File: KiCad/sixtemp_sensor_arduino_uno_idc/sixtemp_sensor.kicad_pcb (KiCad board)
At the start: 2 copper layers, 53.3 x 68.6 mm, 44 parts, among them J10 debug, J12 Sig_conn, J123456 Led_EN, J13 RB_Conn, J31 1-Wire, J32 1-Wire, J33 1-Wire, J34 1-Wire, J35 1-Wire, J36 1-Wire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

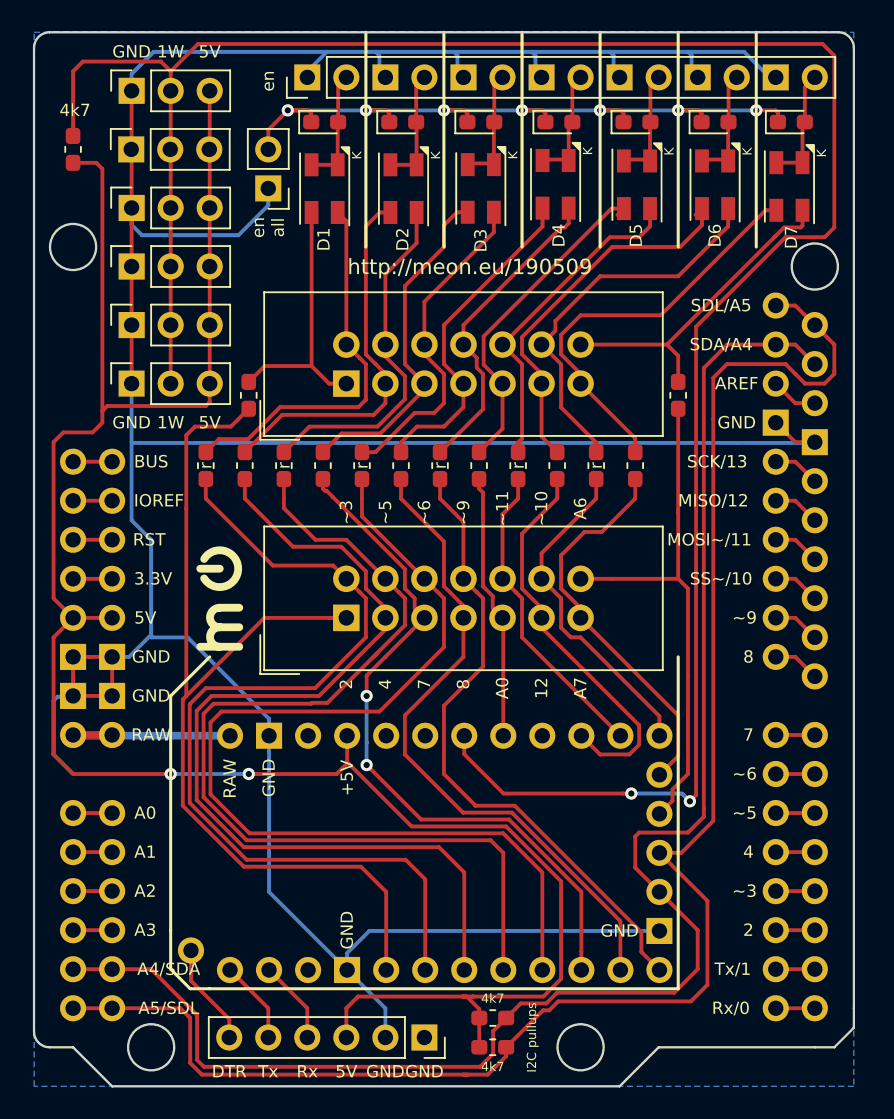
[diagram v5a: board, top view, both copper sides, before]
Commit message: A6→A3, A7→A2 and set as alarm
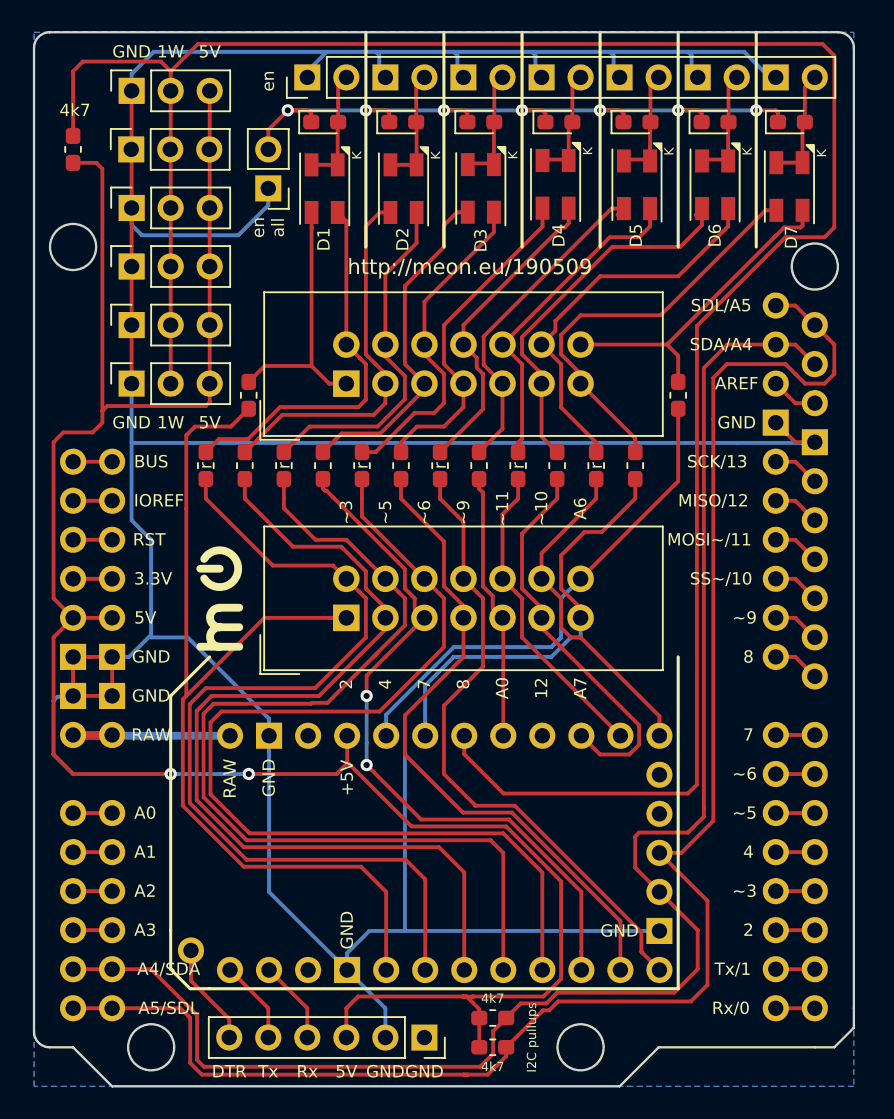
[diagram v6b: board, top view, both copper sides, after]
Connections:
- J12 pad 13: A7 -> A2
- J12 pad 14: A6 -> A3
- R71 pad 2: A6 -> A3
- R72 pad 2: A7 -> A2
- U1 pad 19: A6 -> Net-(U1-Pad19)
- U1 pad 22: A7 -> Net-(U1-Pad22)
- U1 pad 25: Net-(U1-Pad25) -> A2
- U1 pad 26: Net-(U1-Pad26) -> A3
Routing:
- net A6: track 33.9 -> 0.00 mm
- net A3: track 0.00 -> 32.9 mm
- net A2: track 0.00 -> 28.9 mm
- net A7: track 26.3 -> 0.00 mm
- net GND: track 230.2 -> 244.2 mm
- net 1wire: track 147.5 -> 145.9 mm, vias 2 -> 0

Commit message: draw lines between connected pin holes
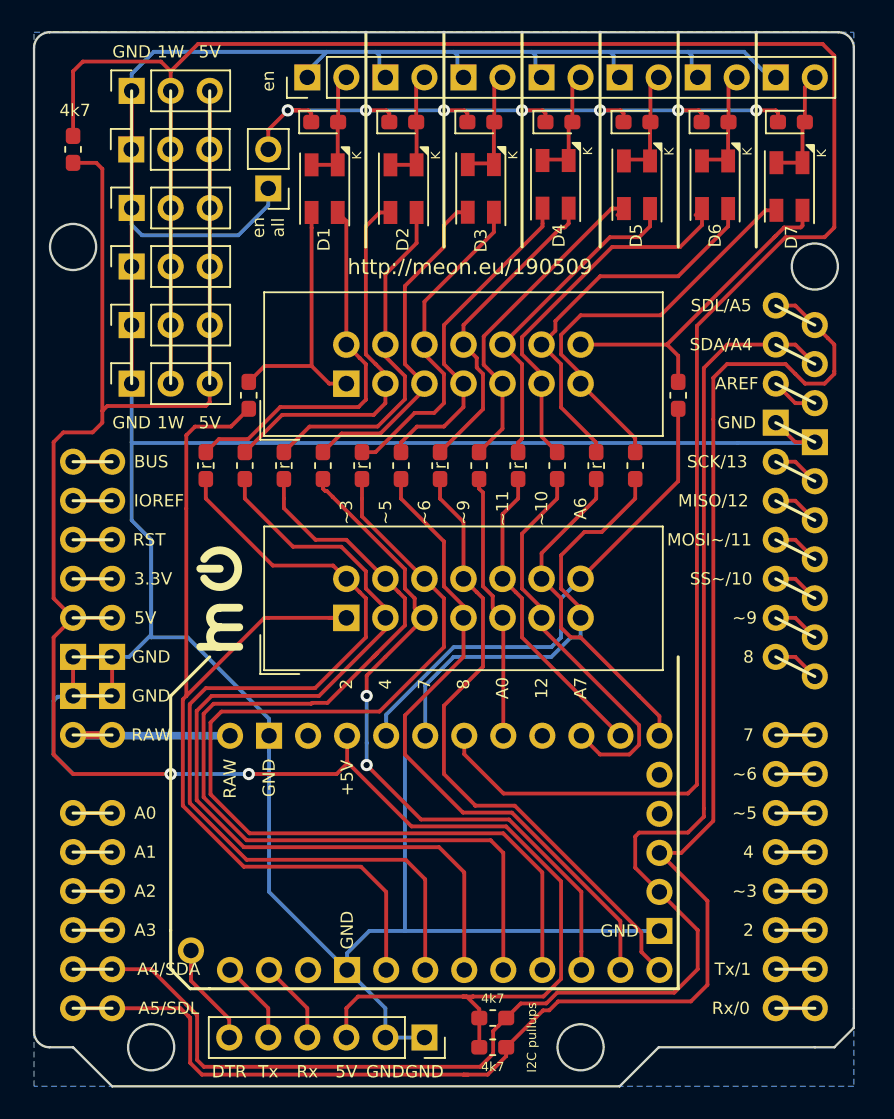
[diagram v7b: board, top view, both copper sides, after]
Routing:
- net GND: track 244.2 -> 246.7 mm
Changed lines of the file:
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@@
   (general
     (thickness 1.6)
-    (drawings 85)
-    (tracks 637)
+    (drawings 120)
+    (tracks 638)
     (zones 0)
     (modules 44)
@@
     (visible_elements FFFFFF7F)
     (pcbplotparams
-      (layerselection 0x010fc_ffffffff)
+      (layerselection 0x010a8_7fffffff)
       (usegerberextensions false)
       (usegerberattributes false)
@@
     )
   )
+  (gr_line (start 68.58 96.52) (end 71.12 96.52) (layer F.SilkS) (width 0.2))
+  (gr_line (start 68.58 93.98) (end 71.12 93.98) (layer F.SilkS) (width 0.2))
+  (gr_line (start 68.58 91.44) (end 71.12 91.44) (layer F.SilkS) (width 0.2))
+  (gr_line (start 68.58 88.9) (end 71.12 88.9) (layer F.SilkS) (width 0.2))
+  (gr_line (start 68.58 86.36) (end 71.12 86.36) (layer F.SilkS) (width 0.2))
+  (gr_line (start 68.58 83.82) (end 71.12 83.82) (layer F.SilkS) (width 0.2))
+  (gr_line (start 114.3 50.8) (end 116.84 52.07) (layer F.SilkS) (width 0.2))
+  (gr_line (start 114.3 53.34) (end 116.84 54.61) (layer F.SilkS) (width 0.2))
+  (gr_line (start 114.3 55.88) (end 116.84 57.15) (layer F.SilkS) (width 0.2))
+  (gr_line (start 114.3 58.42) (end 116.84 59.69) (layer F.SilkS) (width 0.2))
+  (gr_line (start 114.3 60.96) (end 116.84 62.23) (layer F.SilkS) (width 0.2))
+  (gr_line (start 114.3 63.5) (end 116.84 64.77) (layer F.SilkS) (width 0.2))
+  (gr_line (start 114.3 66.04) (end 116.84 67.31) (layer F.SilkS) (width 0.2))
+  (gr_line (start 114.3 68.58) (end 116.84 69.85) (layer F.SilkS) (width 0.2))
+  (gr_line (start 114.3 71.12) (end 116.84 72.39) (layer F.SilkS) (width 0.2))
+  (gr_line (start 114.3 73.66) (end 116.84 74.93) (layer F.SilkS) (width 0.2))
+  (gr_line (start 114.3 78.74) (end 116.84 78.74) (layer F.SilkS) (width 0.2))
+  (gr_line (start 114.3 81.28) (end 116.84 81.28) (layer F.SilkS) (width 0.2))
+  (gr_line (start 114.3 83.82) (end 116.84 83.82) (layer F.SilkS) (width 0.2))
+  (gr_line (start 114.3 86.36) (end 116.84 86.36) (layer F.SilkS) (width 0.2))
+  (gr_line (start 114.3 88.9) (end 116.84 88.9) (layer F.SilkS) (width 0.2))
+  (gr_line (start 114.3 91.44) (end 116.84 91.44) (layer F.SilkS) (width 0.2))
+  (gr_line (start 114.3 93.98) (end 116.84 93.98) (layer F.SilkS) (width 0.2))
+  (gr_line (start 114.3 96.52) (end 116.84 96.52) (layer F.SilkS) (width 0.2))
+  (gr_line (start 68.58 78.74) (end 71.12 78.74) (layer F.SilkS) (width 0.2))
+  (gr_line (start 68.58 76.2) (end 71.12 76.2) (layer F.SilkS) (width 0.2))
+  (gr_line (start 68.58 73.66) (end 71.12 73.66) (layer F.SilkS) (width 0.2))
+  (gr_line (start 68.58 71.12) (end 71.12 71.12) (layer F.SilkS) (width 0.2))
+  (gr_line (start 68.58 68.58) (end 71.12 68.58) (layer F.SilkS) (width 0.2))
+  (gr_line (start 71.12 66.04) (end 68.58 66.04) (layer F.SilkS) (width 0.2))
+  (gr_line (start 68.58 63.5) (end 71.12 63.5) (layer F.SilkS) (width 0.2))
+  (gr_line (start 68.58 60.96) (end 71.12 60.96) (layer F.SilkS) (width 0.2))
+  (gr_line (start 72.39 36.83) (end 72.39 55.88) (layer F.SilkS) (width 0.2))
+  (gr_line (start 74.93 55.88) (end 74.93 36.83) (layer F.SilkS) (width 0.2))
+  (gr_line (start 77.47 36.83) (end 77.47 55.88) (layer F.SilkS) (width 0.2))
   (gr_text r (at 102.616 61.214 90) (layer F.SilkS)
     (effects (font (size 0.8 0.8) (thickness 0.125)))
@@
   (segment (start 106.730801 91.490801) (end 90.17 91.490801) (width 0.25) (layer B.Cu) (net 1))
   (segment (start 90.17 91.490801) (end 87.850801 91.490801) (width 0.25) (layer B.Cu) (net 1))
+  (segment (start 88.9 98.425) (end 91.44 98.425) (width 0.25) (layer B.Cu) (net 1))
   (segment (start 74.93 55.879337) (end 74.929337 55.88) (width 0.25) (layer F.Cu) (net 2))
   (segment (start 74.93 36.83) (end 74.93 55.879337) (width 0.25) (layer F.Cu) (net 2))
@@
   (segment (start 83.82 96.52) (end 81.330801 94.030801) (width 0.25) (layer F.Cu) (net 63))
   (segment (start 83.82 96.52) (end 83.82 98.425) (width 0.25) (layer F.Cu) (net 63))
-  (segment (start 101.6 71.12) (end 101.6 70.33913) (width 0.25) (layer F.Cu) (net 70))
-  (segment (start 102.983 65.532) (end 105.156 63.359) (width 0.25) (layer F.Cu) (net 70))
-  (segment (start 105.156 63.359) (end 105.156 62.089) (width 0.25) (layer F.Cu) (net 70))
-  (segment (start 101.854 65.532) (end 102.983 65.532) (width 0.25) (layer F.Cu) (net 70))
-  (segment (start 101.6 70.48359) (end 100.33 69.21359) (width 0.25) (layer F.Cu) (net 70))
-  (segment (start 100.33 69.21359) (end 100.33 67.056) (width 0.25) (layer F.Cu) (net 70))
-  (segment (start 101.6 71.12) (end 101.6 70.48359) (width 0.25) (layer F.Cu) (net 70))
-  (segment (start 100.33 67.056) (end 101.854 65.532) (width 0.25) (layer F.Cu) (net 70))
   (segment (start 114.339 41.503) (end 116.039 41.503) (width 0.25) (layer F.Cu) (net 64))
   (segment (start 116.191 36.604) (end 116.84 35.955) (width 0.25) (layer F.Cu) (net 64))
@@
   (segment (start 116.039 45.603) (end 115.922 45.72) (width 0.25) (layer F.Cu) (net 66))
   (segment (start 107.95 55.767) (end 107.95 54.069) (width 0.25) (layer F.Cu) (net 66))
+  (segment (start 101.6 71.12) (end 101.6 70.33913) (width 0.25) (layer F.Cu) (net 70))
+  (segment (start 102.983 65.532) (end 105.156 63.359) (width 0.25) (layer F.Cu) (net 70))
+  (segment (start 105.156 63.359) (end 105.156 62.089) (width 0.25) (layer F.Cu) (net 70))
+  (segment (start 101.854 65.532) (end 102.983 65.532) (width 0.25) (layer F.Cu) (net 70))
+  (segment (start 101.6 70.48359) (end 100.33 69.21359) (width 0.25) (layer F.Cu) (net 70))
+  (segment (start 100.33 69.21359) (end 100.33 67.056) (width 0.25) (layer F.Cu) (net 70))
+  (segment (start 101.6 71.12) (end 101.6 70.48359) (width 0.25) (layer F.Cu) (net 70))
+  (segment (start 100.33 67.056) (end 101.854 65.532) (width 0.25) (layer F.Cu) (net 70))
   (segment (start 91.490801 78.790801) (end 91.490801 75.515609) (width 0.25) (layer B.Cu) (net 70))
   (segment (start 91.490801 75.515609) (end 93.345705 73.660705) (width 0.25) (layer B.Cu) (net 70))
